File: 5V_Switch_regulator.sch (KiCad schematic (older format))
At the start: 13 parts, among them U4 MAX17502

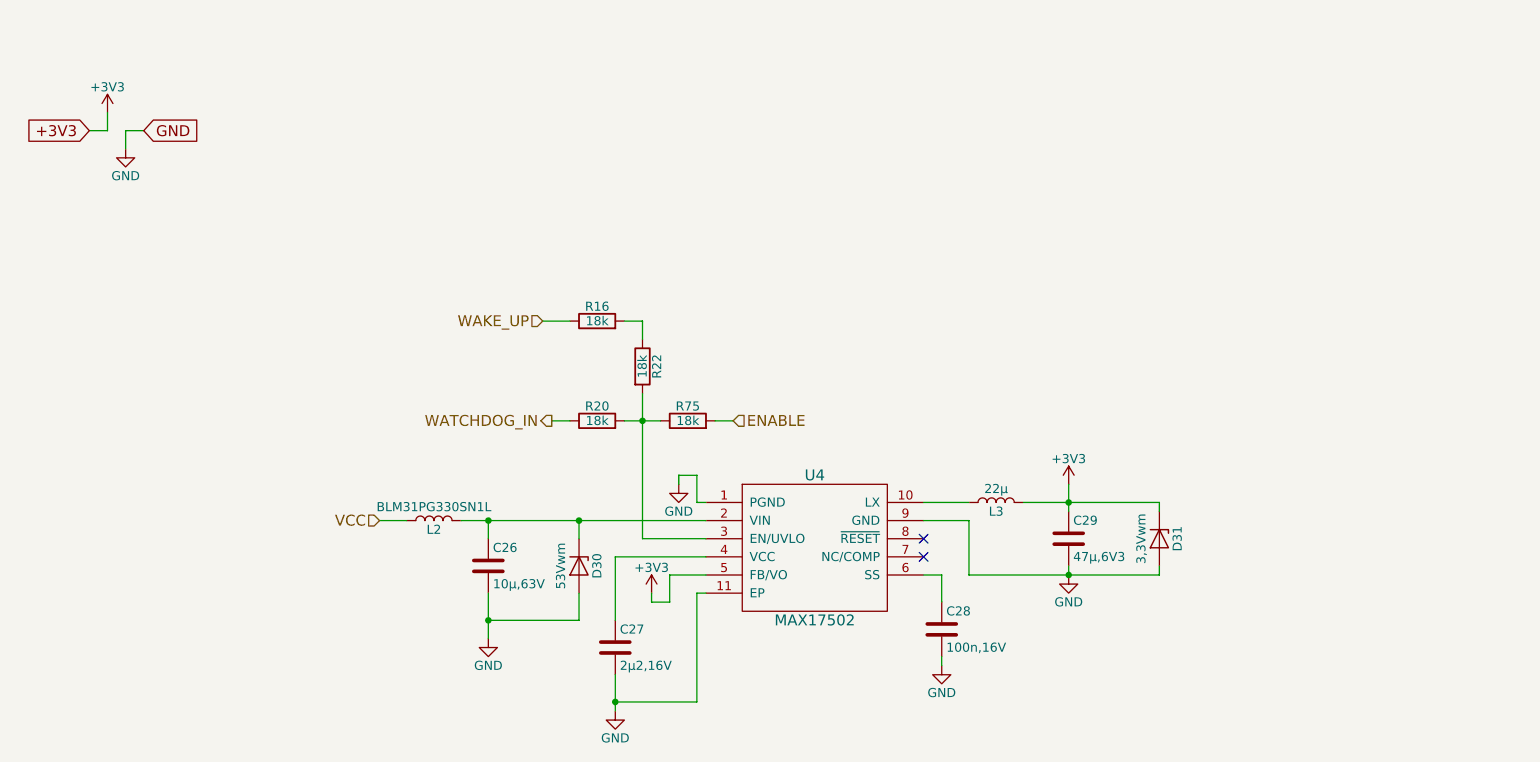
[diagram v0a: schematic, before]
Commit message: HW 0.2 finalized schematic and pcb files, BOM needs to be checked
Lots of major and little problems fixed found in the 0.1

Major changes:
-LTC6803-3 footprint changed to it's correct one
-Boost converter layout and capacitor optimization
-MCU switched from STM32F070CBT6 to ultra low power STM32L433CCT6 to improve sleep state power consumption
-Button/LED + Comms connectors switched from THT JST-XH to SMD JST-PH
-CAN-bus support added
-Changed power regulator setup for "always on"

Minor changes:
-Changed cell balance resistor sizes from 0603 to 0402 in order to get a bit more breathing room during soldering
-External oscillator removed from MCU, because new one has everything available internally
-Comms connector has USART or CAN available via solder bridges
-Sense resistors switched to higher resistance ones to lower deep sleep standby current
-etc.
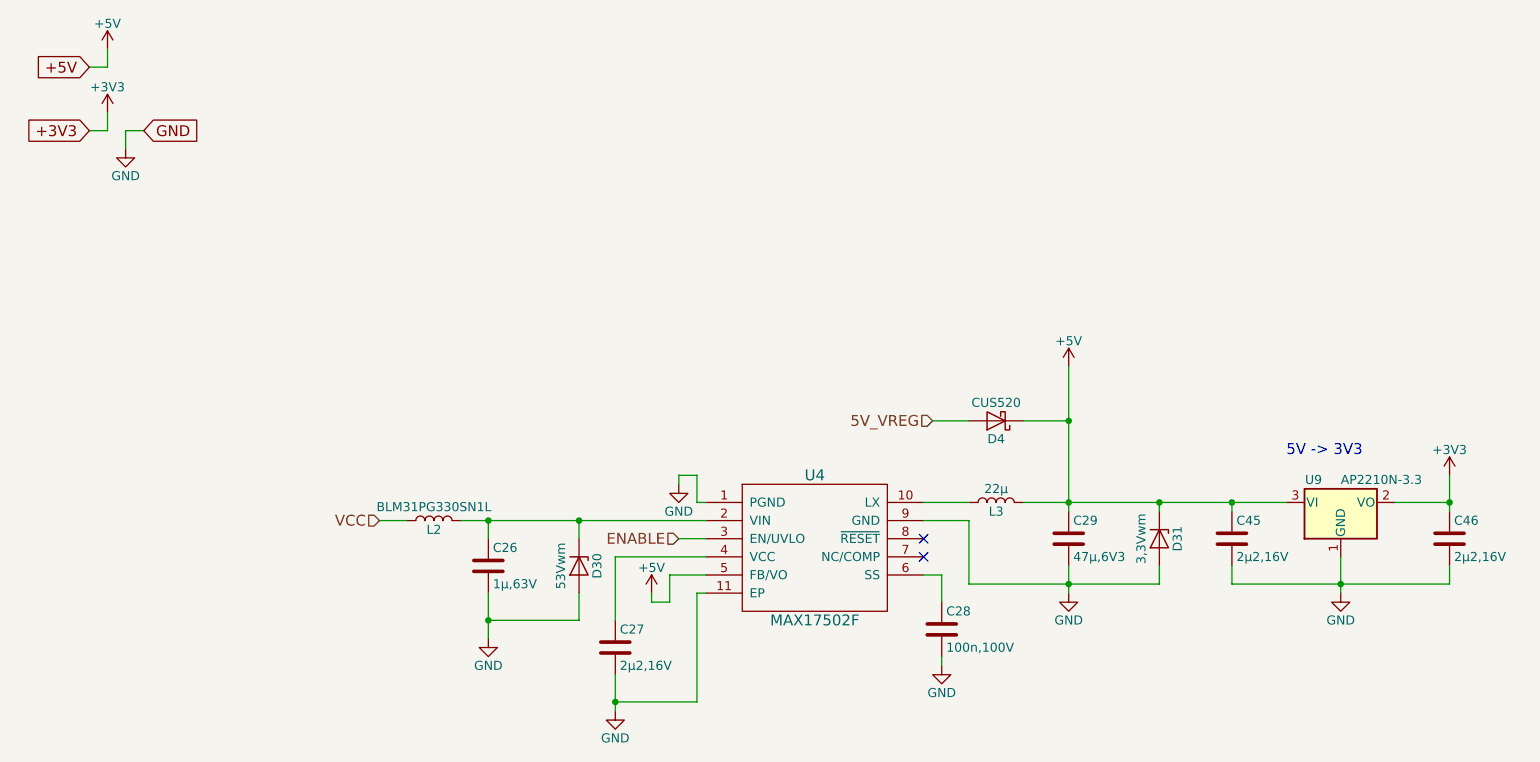
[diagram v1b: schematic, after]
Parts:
- removed R16, R20, R22, R75: 18k, Resistors_SMD:R_0603, symbol R
- added C45, C46: 2µ2,16V, Capacitors_SMD:C_0603, symbol C
- added D4: CUS520, Diodes_SMD:D_SOD-323, symbol D_Schottky
- added U9: AP2210N-3.3, TO_SOT_Packages_SMD:SOT-23, symbol AP1117-15
- C26: value 10µ,63V -> 1µ,63V; footprint Capacitors_SMD:C_1206 -> Capacitors_SMD:C_1210; MFG (none) -> ANY
- C27: MFG EMK107BJ225KA-T -> ANY; TempCo. (none) -> X5R
- C28: value 100n,16V -> 100n,100V; MFG CL10B104KC8NNNC -> ANY; TempCo. (none) -> X7R
- C29: MFG CL31A476MQHNNNE -> ANY; TempCo. (none) -> X5R
- D30: footprint Diodes_SMD:D_SMC -> Diodes_SMD:D_SMA; MFG 1.5SMC62A -> P4SMA62A-E3/61
- U4: value MAX17502 -> MAX17502F; MFG MAX17502EATB+T -> MAX17502FATB+T
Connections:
- net +3V3: now also C46.1, U9.2 (VO); no longer C29.1, D31.1 (K), L3.2, U4.5 (FB/VO)
- net ENABLE: now also U4.3 (EN/UVLO)
- net GND: now also C45.2, C46.2, U9.1 (GND)
- new net +5V: C29.1, C45.1, D31.1 (K), D4.1 (K), L3.2, U4.5 (FB/VO), U9.3 (VI)
- new net 5V_VREG: D4.2 (A)
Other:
- note added: "5V -> 3V3"
